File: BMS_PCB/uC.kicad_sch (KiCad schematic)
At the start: 2 parts, among them J2 Conn_01x15, U7 STM32F407G-DISC1

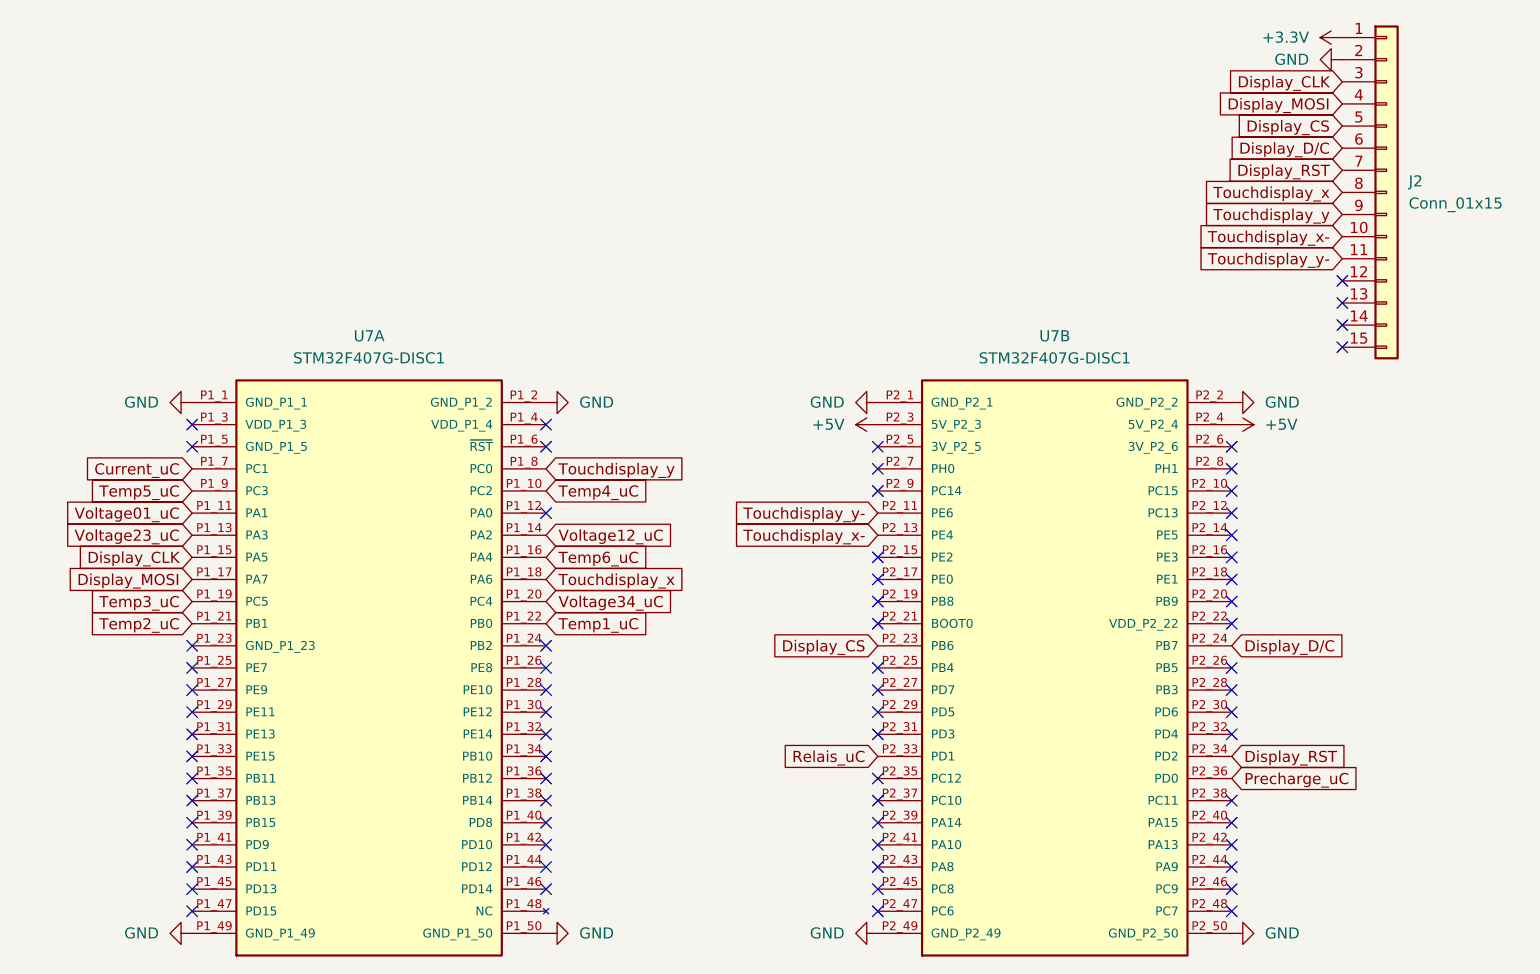
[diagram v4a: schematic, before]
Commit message: schematic uC
changes schematic uC
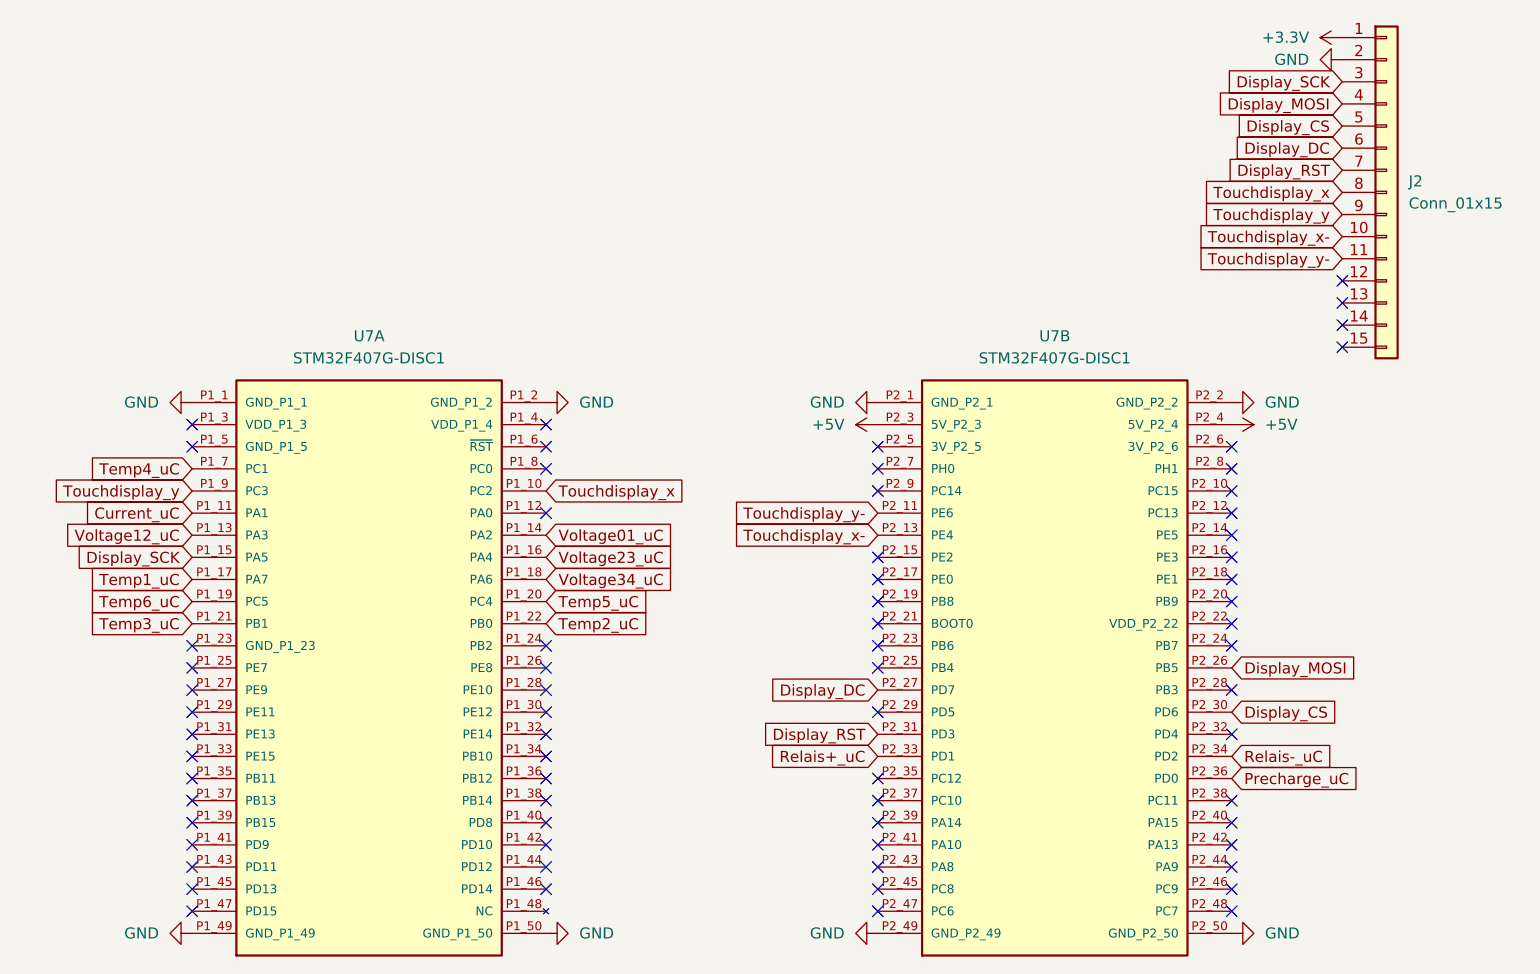
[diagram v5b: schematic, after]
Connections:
- net Current_uC: now also U7.P1_11 (PA1); no longer U7.P1_7 (PC1)
- net Display_CS: now also U7.P2_30 (PD6); no longer U7.P2_23 (PB6)
- net Display_MOSI: now also U7.P2_26 (PB5); no longer U7.P1_17 (PA7)
- net Display_RST: now also U7.P2_31 (PD3); no longer U7.P2_34 (PD2)
- net Temp1_uC: now also U7.P1_17 (PA7); no longer U7.P1_22 (PB0)
- net Temp2_uC: now also U7.P1_22 (PB0); no longer U7.P1_21 (PB1)
- net Temp3_uC: now also U7.P1_21 (PB1); no longer U7.P1_19 (PC5)
- net Temp4_uC: now also U7.P1_7 (PC1); no longer U7.P1_10 (PC2)
- net Temp5_uC: now also U7.P1_20 (PC4); no longer U7.P1_9 (PC3)
- net Temp6_uC: now also U7.P1_19 (PC5); no longer U7.P1_16 (PA4)
- net Touchdisplay_x: now also U7.P1_10 (PC2); no longer U7.P1_18 (PA6)
- net Touchdisplay_y: now also U7.P1_9 (PC3); no longer U7.P1_8 (PC0)
- net Voltage01_uC: now also U7.P1_14 (PA2); no longer U7.P1_11 (PA1)
- net Voltage12_uC: now also U7.P1_13 (PA3); no longer U7.P1_14 (PA2)
- net Voltage23_uC: now also U7.P1_16 (PA4); no longer U7.P1_13 (PA3)
- net Voltage34_uC: now also U7.P1_18 (PA6); no longer U7.P1_20 (PC4)
- net Display_DC: now reaches U7.P2_27 (PD7)
- net Display_DC: now also J2.6 (Pin_6)
- net Display_CLK renamed Display_SCK
- net Display_D/C: no longer names the net of U7.P2_24 (PB7)
- net Display_D/C: no longer J2.6 (Pin_6)
- net Relais_uC renamed Relais+_uC
- new net Relais-_uC: U7.P2_34 (PD2)
- no-connect marks 71 -> 70
